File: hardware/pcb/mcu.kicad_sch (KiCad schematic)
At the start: 65 parts, among them J100 Conn_02x05_Odd_Even, U100 MIMXRT1176DVMAA, Y100 24MHz, Y101 32.768K

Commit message: - Working on pcb layout
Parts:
- removed J100: Conn_02x05_Odd_Even, Connector_PinHeader_1.27mm:PinHeader_2x05_P1.27mm_Vertical_SMD, symbol Connector_Generic:Conn_02x05_Odd_Even
- added C146: 100nF, Capacitor_SMD:C_0201_0603Metric, symbol Device:C
- added J101: Conn_01x04, Connector_PinHeader_1.27mm:PinHeader_1x04_P1.27mm_Vertical_SMD_Pin1Left, symbol Connector_Generic:Conn_01x04
- added U8: PCA9555AHF, Package_DFN_QFN:HVQFN-24-1EP_4x4mm_P0.5mm_EP2.5x2.5mm, symbol symbols:PCA9555AHF
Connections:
- net +1V8: now also C146.1, U8.21 (VDD)
- net GND: now also C146.2, J101.4 (Pin_4), U8.18 (A0), U8.23 (A1), U8.24 (A2), U8.9 (VSS)
- net I2C1_SCL: now also U8.19 (SCL)
- net I2C1_SDA: now also U8.20 (SDA)
- net JTAG_TCK: now also J101.2 (Pin_2)
- net JTAG_TMS: now also J101.1 (Pin_1)
- net RESET: now also J101.3 (Pin_3)
- net JTAG_TDI: no longer names the net of U100.U5 (GPIO_LPSR_12)
- net JTAG_TDO: no longer names the net of U100.T5 (GPIO_LPSR_11)
- net JTAG_TRSTB: no longer names the net of U100.R5 (GPIO_LPSR_10)
- new net DP_PWR_EN: U8.8 (IO0_7)
- new net FPGA_DONE: U8.1 (IO0_0)
- new net FPGA_INIT: U8.5 (IO0_4)
- new net FPGA_KEY_EN: U8.6 (IO0_5)
- new net FPGA_PWR_EN: U8.7 (IO0_6)
- new net FPGA_RST: U8.2 (IO0_1)
- new net KEY_A: U8.17 (IO1_7)
- new net KEY_B: U8.10 (IO1_0)
- new net KEY_DOWN: U8.11 (IO1_1)
- new net KEY_LEFT: U8.12 (IO1_2)
- new net KEY_RIGHT: U8.13 (IO1_3)
- new net KEY_SELECT: U8.16 (IO1_6)
- new net KEY_START: U8.15 (IO1_5)
- new net KEY_UP: U8.14 (IO1_4)
- no-connect marks 20 -> 70
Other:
- moved on the sheet: C100, C101, C102, C103, C104, C105, C106, C107, C108, C109, C110, C111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

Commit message: - PCB r0.3 routed, need to finalize
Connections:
- net FPGA_RAM_EN: now reaches U8.4 (IO0_3)
- net LCD_BL_PWM: now reaches U100.L17 (GPIO_AD_28)
- net KEY_CW: now reaches U100.M17 (GPIO_AD_29)
- net KEY_CCW: now reaches U100.N16 (GPIO_AD_27)
- net VBUS renamed VBUS_IN
- no-connect marks 70 -> 66
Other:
- moved on the sheet: R102, R103

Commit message: - PCB layout finished for r0p3
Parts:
- removed C112: 1uF, Capacitor_SMD:C_0402_1005Metric, symbol Device:C
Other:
- note added: "ADC is not used Decoupling Cap omitted"
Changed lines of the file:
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@@
   (junction (at 373.38 96.52) (diameter 0.9144) (color 0 0 0 0))
   (junction (at 373.38 104.14) (diameter 0.9144) (color 0 0 0 0))
-  (junction (at 375.92 137.16) (diameter 0.9144) (color 0 0 0 0))
   (junction (at 383.54 86.36) (diameter 0.9144) (color 0 0 0 0))
   (junction (at 383.54 93.98) (diameter 0.9144) (color 0 0 0 0))
@@
     (effects (font (size 1.27 1.27)) (justify right bottom))
   )
+  (text "ADC is not used\nDecoupling Cap omitted" (at 392.43 143.51 180)
+    (effects (font (size 1.27 1.27)) (justify right bottom))
+  )
   (label "RESET" (at 170.18 213.36 0)
     (effects (font (size 1.27 1.27)) (justify left bottom))
@@
     (pin "1")
   )
-  (symbol (lib_id "power:GND") (at 375.92 144.78 0) (unit 1)
-    (in_bom yes) (on_board yes)
-    (property "Reference" "#PWR0113" (id 0) (at 375.92 151.13 0)
-      (effects (font (size 1.27 1.27)) hide)
-    )
-    (property "Value" "GND" (id 1) (at 376.047 149.1742 0))
-    (property "Footprint" "" (id 2) (at 375.92 144.78 0)
-      (effects (font (size 1.27 1.27)) hide)
-    )
-    (property "Datasheet" "" (id 3) (at 375.92 144.78 0)
-      (effects (font (size 1.27 1.27)) hide)
-    )
-    (pin "1")
-  )
   (symbol (lib_id "power:GND") (at 378.46 167.64 0) (unit 1)
     (in_bom yes) (on_board yes)
@@
       (effects (font (size 1.27 1.27)) hide)
     )
-    (pin "1")
-    (pin "2")
-  )
-  (symbol (lib_id "Device:C") (at 375.92 140.97 0) (unit 1)
-    (in_bom yes) (on_board yes)
-    (property "Reference" "C112" (id 0) (at 378.841 139.802 0)
-      (effects (font (size 1.27 1.27)) (justify left))
-    )
-    (property "Value" "1uF" (id 1) (at 378.841 142.113 0)
-      (effects (font (size 1.27 1.27)) (justify left))
-    )
-    (property "Footprint" "Capacitor_SMD:C_0402_1005Metric" (id 2) (at 376.8852 144.78 0)
-      (effects (font (size 1.27 1.27)) hide)
-    )
-    (property "Datasheet" "~" (id 3) (at 375.92 140.97 0)
-      (effects (font (size 1.27 1.27)) hide)
-    )

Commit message: - PCB: prepare for r0p4
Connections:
- net SAI4_RX_DATA: now reaches U100.P8 (GPIO_LPSR_06)
- net SAI4_RX_BCLK: now reaches U100.R8 (GPIO_LPSR_07)
- net SAI4_RX_SYNC: now reaches U100.U8 (GPIO_LPSR_08)
- net SAI1_MCLK: no longer names the net of U100.D7 (GPIO_DISP_B2_03)
- net SAI1_RX_BCLK: no longer names the net of U100.C9 (GPIO_DISP_B2_05)
- net SAI1_RX_DATA0: no longer names the net of U100.C6 (GPIO_DISP_B2_06)
- net SAI1_RX_SYNC: no longer names the net of U100.C7 (GPIO_DISP_B2_04)
- net SAI4_TX_BCLK: no longer names the net of U100.N7 (GPIO_LPSR_04)
- net SAI4_TX_DATA: no longer names the net of U100.P6 (GPIO_LPSR_02)
- net SAI4_TX_SYNC: no longer names the net of U100.T7 (GPIO_LPSR_03)
- no-connect marks 66 -> 70

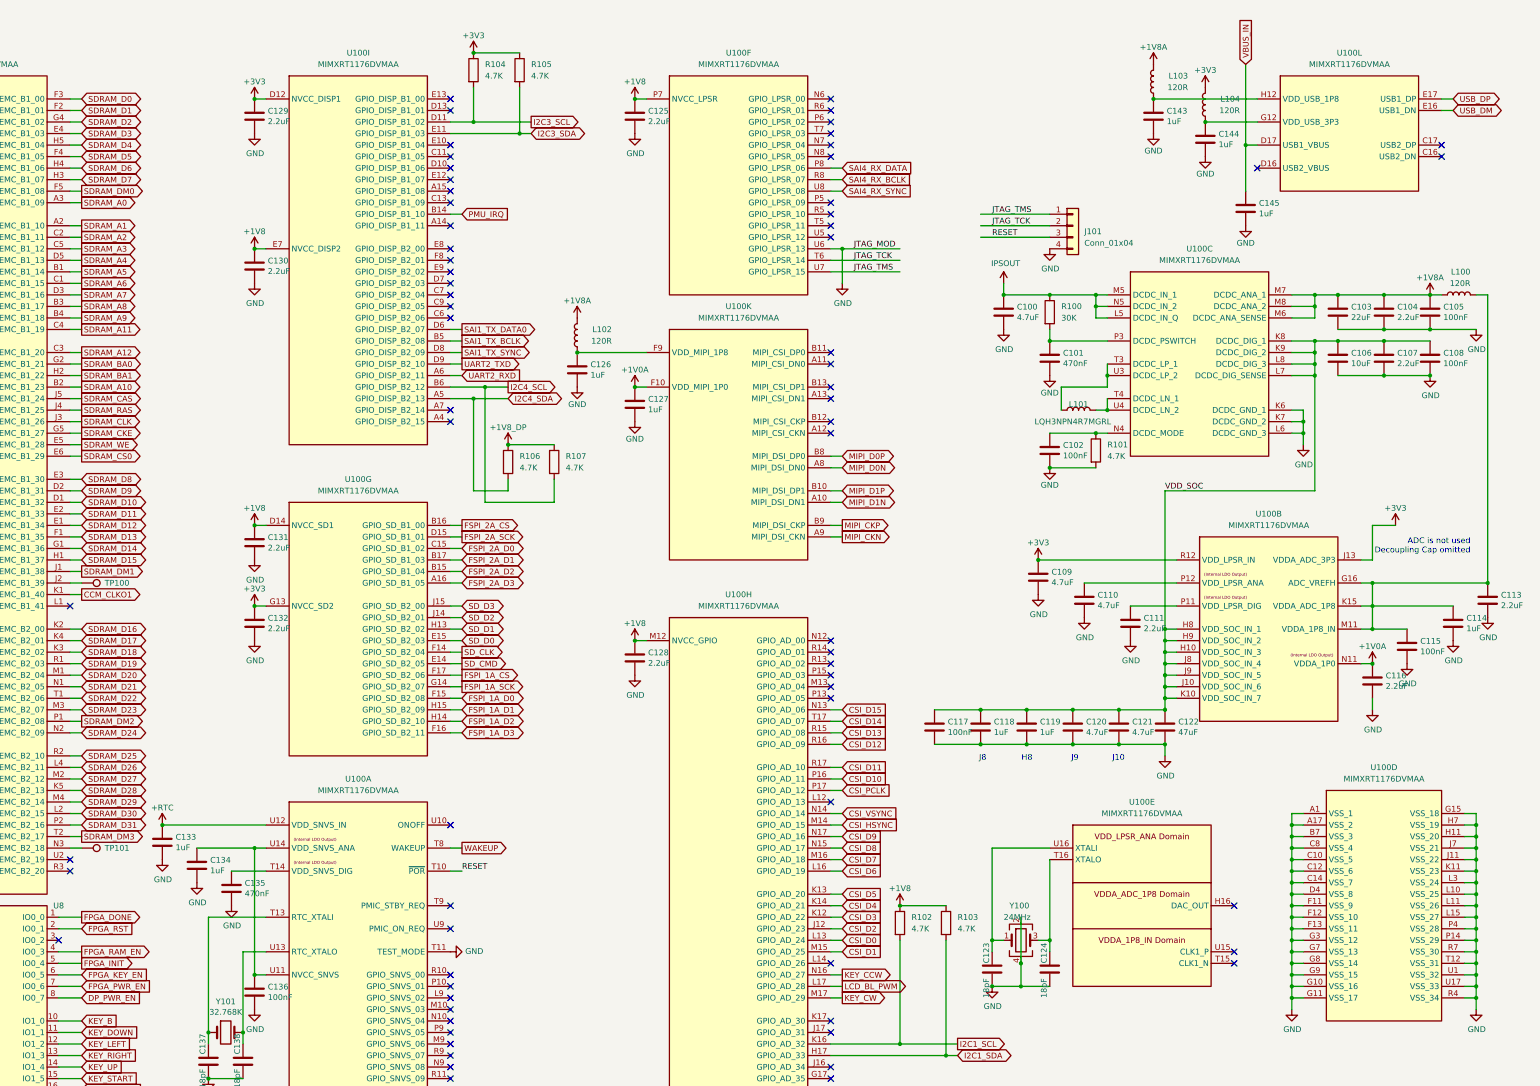
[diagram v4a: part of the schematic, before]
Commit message: - pcb: r0p4, update to KiCAD 6.0
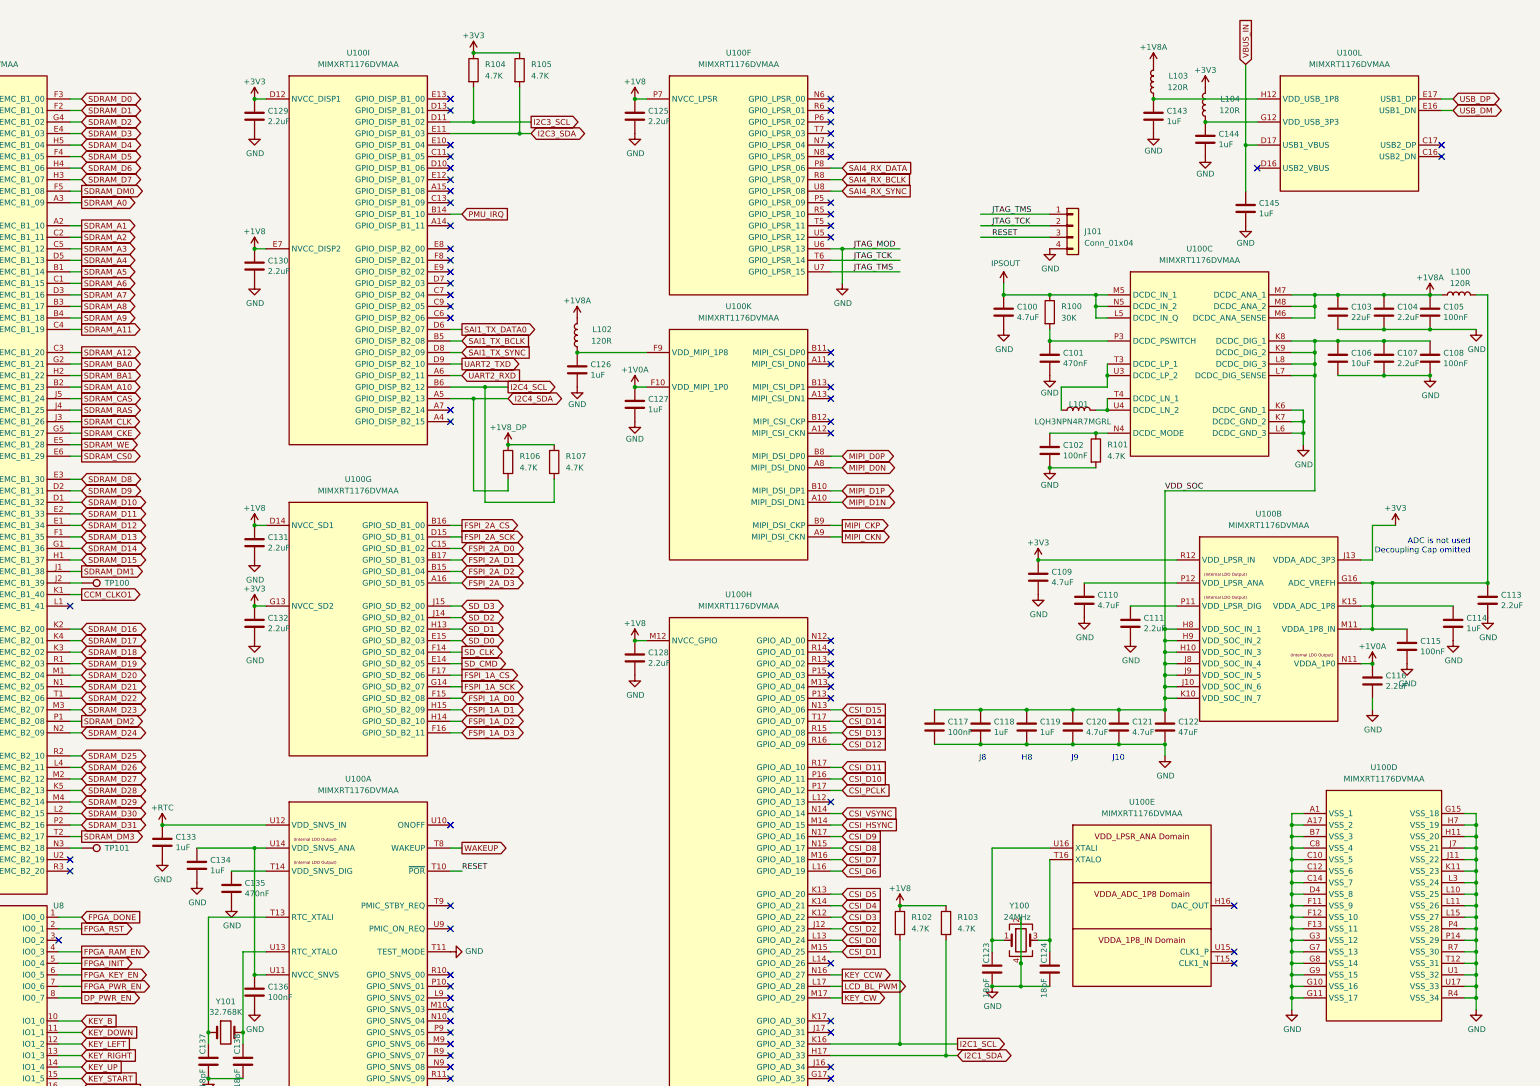
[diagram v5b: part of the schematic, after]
